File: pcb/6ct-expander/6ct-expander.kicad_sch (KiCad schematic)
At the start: 3 parts, among them J7 Conn_02x05_Odd_Even

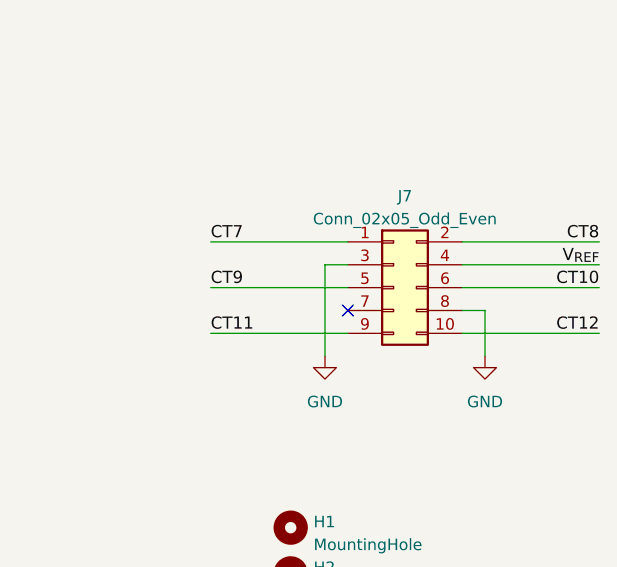
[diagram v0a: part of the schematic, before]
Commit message: [6CT] Mirror connector pins to match emonPi3 pin out
  - Mirrored to emonPi3 pin out facing *down*
  - Also update board information
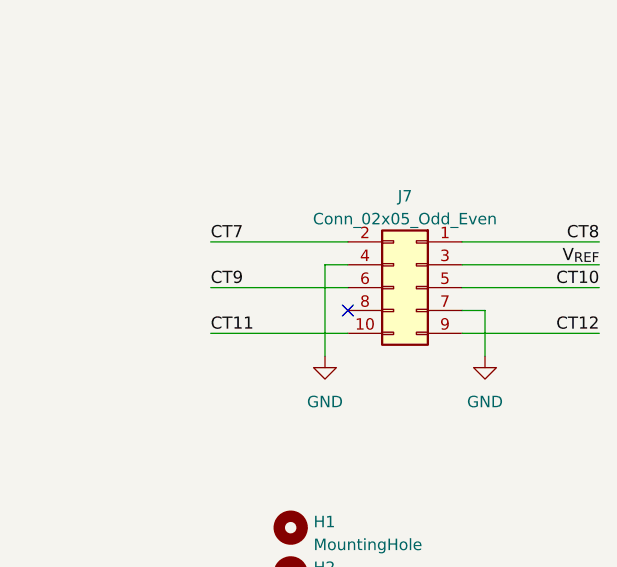
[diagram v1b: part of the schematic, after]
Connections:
- net CT10: now also J7.5 (Pin_5); no longer J7.6 (Pin_6)
- net CT11: now also J7.10 (Pin_10); no longer J7.9 (Pin_9)
- net CT12: now also J7.9 (Pin_9); no longer J7.10 (Pin_10)
- net CT7: now also J7.2 (Pin_2); no longer J7.1 (Pin_1)
- net CT8: now also J7.1 (Pin_1); no longer J7.2 (Pin_2)
- net CT9: now also J7.6 (Pin_6); no longer J7.5 (Pin_5)
- net GND: now also J7.4 (Pin_4), J7.7 (Pin_7); no longer J7.3 (Pin_3), J7.8 (Pin_8)
- net V_{REF}: now also J7.3 (Pin_3); no longer J7.4 (Pin_4)
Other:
- company: (none) -> OpenEnergyMonitor / Tilt Ltd
- title: (none) -> emonPi3 / Tx6 6CT expander
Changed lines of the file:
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@@
 	(generator_version "9.0")
 	(paper "A4")
+	(title_block
+		(title "emonPi3 / Tx6 6CT expander")
+		(date "2025-12-10")
+		(rev "v1.1")
+		(company "OpenEnergyMonitor / Tilt Ltd")
+		(comment 1 "Angus Logan, 2025")
+	)
 	(no_connect
 		(at 144.78 90.17)
@@
 	(wire
 		(pts
+			(xy 129.54 92.71) (xy 144.78 92.71)
+		)
+		(stroke
+			(width 0.1524)
+			(type solid)
+		)
+	)
+	(wire
+		(pts
 			(xy 58.42 58.42) (xy 71.12 58.42)
 		)
@@
 	(wire
 		(pts
-			(xy 129.54 92.71) (xy 144.78 92.71)
-		)
-		(stroke
-			(width 0.1524)
-			(type solid)
-		)
-	)
-	(wire
-		(pts
 			(xy 58.42 97.79) (xy 71.12 97.79)
 		)
@@
 	(wire
 		(pts
+			(xy 142.24 85.09) (xy 142.24 95.25)
+		)
+		(stroke
+			(width 0)
+			(type default)
+		)
+	)
+	(wire
+		(pts
 			(xy 157.48 85.09) (xy 172.72 85.09)
 		)
@@
 		(pts
 			(xy 144.78 85.09) (xy 142.24 85.09)
-		)
-		(stroke
-			(width 0)
-			(type default)
-		)
-	)
-	(wire
-		(pts
-			(xy 142.24 85.09) (xy 142.24 95.25)
 		)
 		(stroke
@@
 	(symbol
 		(lib_id "Connector_Generic:Conn_02x05_Odd_Even")
-		(at 149.86 87.63 0)
+		(at 152.4 87.63 0)
+		(mirror y)
 		(unit 1)
 		(exclude_from_sim no)
@@
 		(on_board yes)
 		(dnp no)
-		(fields_autoplaced yes)
 		(property "Reference" "J7"
 			(at 151.13 77.47 0)
@@
 		)
 		(property "Footprint" "Connector_PinHeader_2.54mm:PinHeader_2x05_P2.54mm_Vertical"
-			(at 149.86 87.63 0)
+			(at 152.4 87.63 0)
 			(effects
 				(font
@@
 		)
 		(property "Datasheet" "~"
-			(at 149.86 87.63 0)
+			(at 152.4 87.63 0)
 			(effects
 				(font
@@
 		)
 		(property "Description" ""
-			(at 149.86 87.63 0)
-			(effects
-				(font
+			(at 152.4 87.63 0)
+			(effects
+				(font
